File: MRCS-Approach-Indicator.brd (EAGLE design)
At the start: 99.8 x 68.8 mm, 30 parts, among them CON1 GND, CON2 GND Jumpers, J1 5 VDC, J2 Output, J3 Station 0, J4 Station 1, J5 Stations 2 and 3, J6 relay out, K1 G6H2-100, K2 G6H2-100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

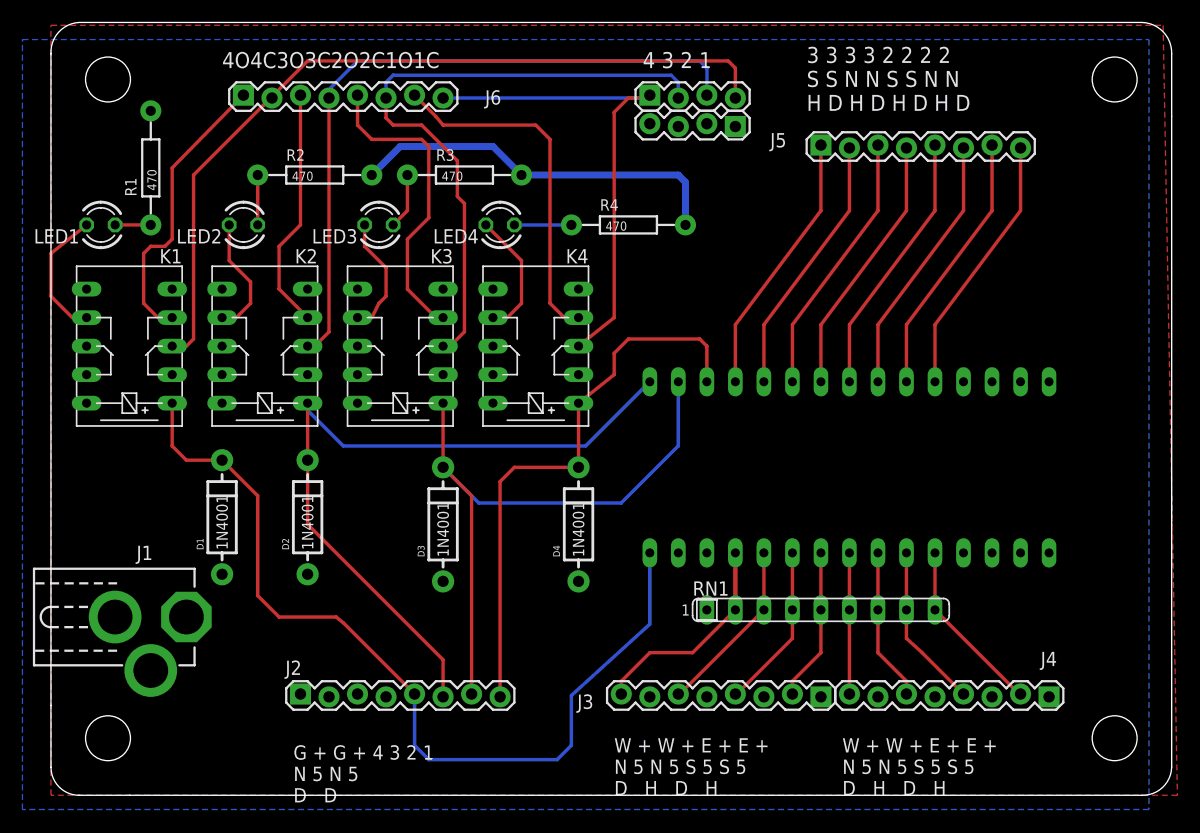
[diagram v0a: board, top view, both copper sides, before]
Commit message: label corrections
changes to labels to align better with code, note some board designations are different than schematic
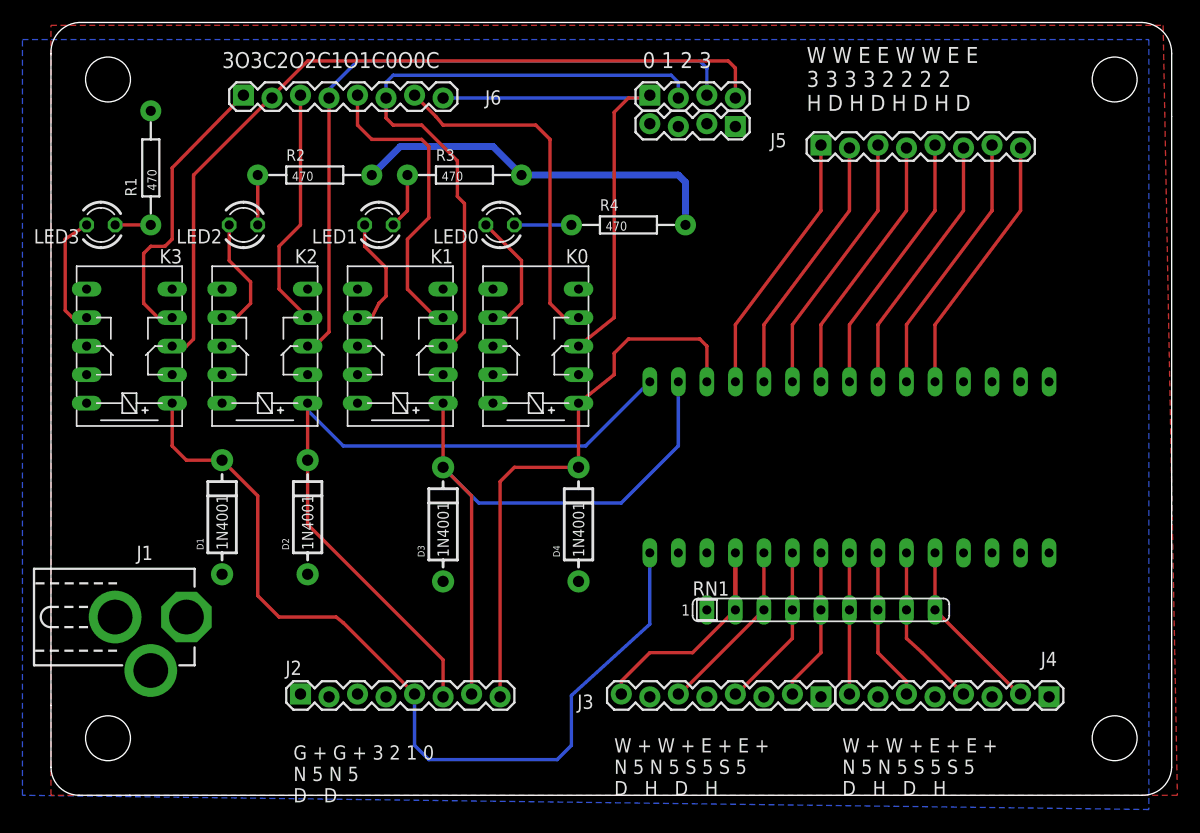
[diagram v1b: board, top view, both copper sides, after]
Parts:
- moved LED1 24.8 mm to (31.8, 52.1)
- moved LED3 24.8 mm to (6.99, 52.1)
- moved K1 24.1 mm to (33.7, 41.3)
- moved K3 24.1 mm to (9.53, 41.3)
- renumbered K4 to K0, LED4 to LED0
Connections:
- net D7: now also K3.1; no longer K1.1
- net N$21: now also K1.S1; no longer K3.S1
- net N$22: now also K3.P1; no longer K1.P1
- net N$23: now also K1.P1; no longer K3.P1
- net N$27: now also LED3.A; no longer LED1.A
- net N$30: now also LED1.A; no longer LED3.A
- net N$34: now also K1.1; no longer K3.1
- net N$7: now also K3.S1; no longer K1.S1
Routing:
- net N$26: track 11.4 -> 10.8 mm
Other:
- board text added: "0 1 2 3"
- board text added: "3O3C2O2C1O1C0O0C"
- board text added: "G + G + 3 2 1 0 N 5 N 5 D D"
- board text added: "V1.1 20211202"
- board text added: "W W E E W W E E 3 3 3 3 2 2 2 2 H D H D H D H D"
- board text removed: "3 3 3 3 2 2 2 2 S S N N S S N N H D H D H D H D"
- board text removed: "4 3 2 1"
- board text removed: "4O4C3O3C2O2C1O1C"
- board text removed: "G + G + 4 3 2 1 N 5 N 5 D D"
- board text removed: "V1.0 20210828"
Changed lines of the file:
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@@
 <text x="84.455" y="48.895" size="1.27" layer="51" font="vector" rot="R180">Seth Neumann
 Jon Schmidt</text>
-<text x="70.485" y="41.91" size="1.4224" layer="51" font="vector">V1.0 20210828</text>
+<text x="70.485" y="41.91" size="1.4224" layer="51" font="vector">V1.1 20211202</text>
 <text x="64.135" y="31.75" size="1.778" layer="51" font="vector">Arduino Nano</text>
 <text x="7.62" y="59.055" size="1.778" layer="22" rot="MR270">Solder Side</text>
@@
 D   H   D   H
 </text>
-<text x="24.13" y="0.635" size="1.27" layer="21" font="vector" ratio="10">G + G + 4 3 2 1
+<text x="24.13" y="0.635" size="1.27" layer="21" font="vector" ratio="10">G + G + 3 2 1 0
 N 5 N 5
 D   D
 </text>
-<text x="17.78" y="66.04" size="1.4224" layer="21" font="vector" ratio="10">4O4C3O3C2O2C1O1C</text>
-<text x="69.85" y="62.23" size="1.4224" layer="21" font="vector" ratio="10">3 3 3 3 2 2 2 2
-S S N N S S N N
+<text x="17.78" y="66.04" size="1.4224" layer="21" font="vector" ratio="10">3O3C2O2C1O1C0O0C</text>
+<text x="69.85" y="62.23" size="1.4224" layer="21" font="vector" ratio="10">W W E E W W E E
+3 3 3 3 2 2 2 2
 H D H D H D H D</text>
-<text x="55.245" y="66.04" size="1.4224" layer="21" font="vector" ratio="10">4 3 2 1</text>
+<text x="55.245" y="66.04" size="1.4224" layer="21" font="vector" ratio="10">0 1 2 3</text>
 </plain>
 <attributes>
@@
 <attribute name="VALUE" x="71.12" y="52.07" size="1.778" layer="27"/>
 </element>
-<element name="K1" library="relay" package="G6H2-100" value="G6H2-100" x="9.525" y="41.275" rot="R90">
+<element name="K3" library="relay" package="G6H2-100" value="G6H2-100" x="9.525" y="41.275" rot="R90">
 <attribute name="OC_NEWARK" value="unknown" x="9.525" y="41.275" size="1.778" layer="27" font="vector" ratio="10" rot="R90" display="off"/>
 <attribute name="OC_FARNELL" value="unknown" x="9.525" y="41.275" size="1.778" layer="27" font="vector" ratio="10" rot="R90" display="off"/>
@@
 <attribute name="MPN" value="" x="21.59" y="41.275" size="1.778" layer="27" font="vector" ratio="10" rot="R90" display="off"/>
 </element>
-<element name="K3" library="relay" package="G6H2-100" value="G6H2-100" x="33.655" y="41.275" rot="R90">
+<element name="K1" library="relay" package="G6H2-100" value="G6H2-100" x="33.655" y="41.275" rot="R90">
 <attribute name="OC_NEWARK" value="unknown" x="33.655" y="41.275" size="1.778" layer="27" font="vector" ratio="10" rot="R90" display="off"/>
 <attribute name="OC_FARNELL" value="unknown" x="33.655" y="41.275" size="1.778" layer="27" font="vector" ratio="10" rot="R90" display="off"/>
@@
 <attribute name="MPN" value="" x="33.655" y="41.275" size="1.778" layer="27" font="vector" ratio="10" rot="R90" display="off"/>
 </element>
-<element name="K4" library="relay" package="G6H2-100" value="G6H2-100" x="45.72" y="41.275" rot="R90">
+<element name="K0" library="relay" package="G6H2-100" value="G6H2-100" x="45.72" y="41.275" rot="R90">
 <attribute name="OC_NEWARK" value="unknown" x="45.72" y="41.275" size="1.778" layer="27" font="vector" ratio="10" rot="R90" display="off"/>
 <attribute name="OC_FARNELL" value="unknown" x="45.72" y="41.275" size="1.778" layer="27" font="vector" ratio="10" rot="R90" display="off"/>
@@
 <attribute name="VALUE" x="11.938" y="55.118" size="0.8128" layer="21" ratio="15" rot="R90"/>
 </element>
-<element name="LED1" library="SPCoast" package="LED3MM" value="RED" x="6.985" y="52.07"/>
+<element name="LED3" library="SPCoast" package="LED3MM" value="RED" x="6.985" y="52.07"/>
 <element name="R2" library="SPCoast" package="AXIAL-0.4-RES" value="470" x="26.035" y="56.515" smashed="yes">
 <attribute name="NAME" x="23.495" y="57.785" size="1.016" layer="25"/>
@@
 <attribute name="VALUE" x="37.338" y="56.007" size="0.8128" layer="21" ratio="15"/>
 </element>
-<element name="LED3" library="SPCoast" package="LED3MM" value="RED" x="31.75" y="52.07"/>
+<element name="LED1" library="SPCoast" package="LED3MM" value="RED" x="31.75" y="52.07"/>
 <element name="R4" library="SPCoast" package="AXIAL-0.4-RES" value="470" x="53.975" y="52.07" smashed="yes">
 <attribute name="NAME" x="51.435" y="53.34" size="1.016" layer="25"/>
 <attribute name="VALUE" x="51.943" y="51.562" size="0.8128" layer="21" ratio="15"/>
 </element>
-<element name="LED4" library="SPCoast" package="LED3MM" value="RED" x="42.545" y="52.07"/>
+<element name="LED0" library="SPCoast" package="LED3MM" value="RED" x="42.545" y="52.07"/>
 </elements>
 <signals>
@@
 <vertex x="100.33" y="68.58"/>
 <vertex x="100.33" y="0"/>
-<vertex x="0" y="0"/>
+<vertex x="0" y="1.27"/>
 </polygon>
 <contactref element="NANO" pad="GND1"/>
 <contactref element="J2" pad="1"/>
+<contactref element="K3" pad="10"/>
+<contactref element="K2" pad="10"/>
 <contactref element="K1" pad="10"/>
-<contactref element="K2" pad="10"/>
-<contactref element="K3" pad="10"/>
-<contactref element="K4" pad="10"/>
+<contactref element="K0" pad="10"/>
 <contactref element="RN1" pad="1"/>
 <contactref element="CON1" pad="1"/>
@@
 <contactref element="CON1" pad="3"/>
 <contactref element="CON1" pad="4"/>
+<contactref element="K3" pad="P2"/>
+<contactref element="K2" pad="P2"/>
 <contactref element="K1" pad="P2"/>
-<contactref element="K2" pad="P2"/>
-<contactref element="K3" pad="P2"/>
-<contactref element="K4" pad="P2"/>
+<contactref element="K0" pad="P2"/>
 <contactref element="J2" pad="3"/>
 <contactref element="D1" pad="A"/>
@@
 <wire x1="47.625" y1="4.445" x2="36.195" y2="4.445" width="0.3048" layer="16"/>
 <wire x1="36.195" y1="4.445" x2="34.925" y2="5.715" width="0.3048" layer="16"/>
-<contactref element="K1" pad="1"/>
+<contactref element="K3" pad="1"/>
 <contactref element="J2" pad="5"/>
 <wire x1="34.925" y1="5.715" x2="34.925" y2="10.287" width="0.3048" layer="16"/>
@@
 <signal name="N$2">
 <contactref element="NANO" pad="D10"/>
-<contactref element="K4" pad="1"/>
+<contactref element="K0" pad="1"/>
 <wire x1="49.53" y1="36.195" x2="52.705" y2="38.735" width="0.3048" layer="1"/>
 <contactref element="J2" pad="8"/>
@@
 </signal>
 <signal name="N$7">
-<contactref element="K1" pad="S1"/>
+<contactref element="K3" pad="S1"/>
 <contactref element="J6" pad="1"/>
 <wire x1="19.685" y1="63.627" x2="13.335" y2="57.15" width="0.3048" layer="1"/>
@@
 </signal>
 <signal name="N$22">
-<contactref element="K1" pad="P1"/>
+<contactref element="K3" pad="P1"/>
 <contactref element="J6" pad="2"/>
 <contactref element="CON2" pad="4"/>
@@
 <signal name="N$21">
 <contactref element="J6" pad="5"/>
-<contactref element="K3" pad="S1"/>
+<contactref element="K1" pad="S1"/>
 <wire x1="37.465" y1="43.815" x2="36.83" y2="43.815" width="0.3048" layer="1"/>
 <wire x1="36.83" y1="43.815" x2="34.29" y2="46.355" width="0.3048" layer="1"/>
@@
 <contactref element="CON2" pad="2"/>
 <contactref element="J6" pad="6"/>
-<contactref element="K3" pad="P1"/>
+<contactref element="K1" pad="P1"/>
 <wire x1="37.465" y1="41.275" x2="38.1" y2="41.275" width="0.3048" layer="1"/>
 <wire x1="38.1" y1="41.275" x2="39.37" y2="42.545" width="0.3048" layer="1"/>
@@
 <signal name="N$25">
 <contactref element="CON2" pad="1"/>
-<contactref element="K4" pad="P1"/>
+<contactref element="K0" pad="P1"/>
 <contactref element="J6" pad="8"/>
 <wire x1="37.465" y1="63.373" x2="55.626" y2="63.373" width="0.3048" layer="16"/>
@@
 <signal name="N$24">
 <contactref element="J6" pad="7"/>
-<contactref element="K4" pad="S1"/>
+<contactref element="K0" pad="S1"/>
 <wire x1="49.53" y1="43.815" x2="48.26" y2="43.815" width="0.3048" layer="1"/>
 <wire x1="48.26" y1="43.815" x2="46.99" y2="45.085" width="0.3048" layer="1"/>
@@
 </signal>
 <signal name="N$27">
-<contactref element="LED1" pad="A"/>
+<contactref element="LED3" pad="A"/>
 <contactref element="R1" pad="P$1"/>
 <wire x1="8.255" y1="52.07" x2="11.43" y2="52.07" width="0.3048" layer="1"/>
 </signal>
 <signal name="N$26">
-<contactref element="K1" pad="S2"/>
-<contactref element="LED1" pad="K"/>
+<contactref element="K3" pad="S2"/>
+<contactref element="LED3" pad="K"/>
 <wire x1="5.715" y1="43.815" x2="4.445" y2="43.815" width="0.3048" layer="1"/>
-<wire x1="4.445" y1="43.815" x2="2.54" y2="45.72" width="0.3048" layer="1"/>
-<wire x1="2.54" y1="45.72" x2="2.54" y2="49.53" width="0.3048" layer="1"/>
-<wire x1="2.54" y1="49.53" x2="5.715" y2="52.07" width="0.3048" layer="1"/>
+<wire x1="4.445" y1="43.815" x2="3.81" y2="44.45" width="0.3048" layer="1"/>
+<wire x1="3.81" y1="44.45" x2="3.81" y2="50.8" width="0.3048" layer="1"/>
+<wire x1="3.81" y1="50.8" x2="5.715" y2="52.07" width="0.3048" layer="1"/>
 </signal>
 <signal name="N$28">
@@
 </signal>
 <signal name="N$30">
-<contactref element="LED3" pad="A"/>
+<contactref element="LED1" pad="A"/>
 <contactref element="R3" pad="P$1"/>
 <wire x1="33.02" y1="52.07" x2="34.29" y2="53.34" width="0.3048" layer="1"/>
@@
 </signal>
 <signal name="N$31">
-<contactref element="LED3" pad="K"/>
-<contactref element="K3" pad="S2"/>
+<contactref element="LED1" pad="K"/>
+<contactref element="K1" pad="S2"/>
 <wire x1="29.845" y1="43.815" x2="29.21" y2="43.815" width="0.3048" layer="1"/>
 <wire x1="30.48" y1="52.07" x2="30.48" y2="50.165" width="0.3048" layer="1"/>
@@
 </signal>
 <signal name="N$32">
-<contactref element="LED4" pad="A"/>
+<contactref element="LED0" pad="A"/>
 <contactref element="R4" pad="P$1"/>
 <wire x1="43.815" y1="52.07" x2="48.895" y2="52.07" width="0.3048" layer="16"/>
 </signal>
 <signal name="N$33">
-<contactref element="LED4" pad="K"/>
-<contactref element="K4" pad="S2"/>
+<contactref element="LED0" pad="K"/>
+<contactref element="K0" pad="S2"/>
 <wire x1="41.91" y1="43.815" x2="41.275" y2="43.815" width="0.3048" layer="1"/>
 <wire x1="41.275" y1="52.07" x2="44.45" y2="48.895" width="0.3048" layer="1"/>
@@
 <signal name="N$34">
 <contactref element="NANO" pad="D11"/>
-<contactref element="K3" pad="1"/>
+<contactref element="K1" pad="1"/>
 <wire x1="58.42" y1="38.1" x2="58.42" y2="32.385" width="0.3048" layer="16"/>
 <wire x1="58.42" y1="32.385" x2="53.34" y2="27.305" width="0.3048" layer="16"/>
